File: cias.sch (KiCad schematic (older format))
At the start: 62 parts, among them CN13 KEYBOARD, CN6 SERIAL_DB25M, CN7 PARALLEL_DB25F, Q501 2N3904, Q502 2N3906, Q503 2N3906, Q711 2N3904, U38 MC1488, U39 MC1489, U42 NE555, U7 VIA_8520, U8 VIA_8520

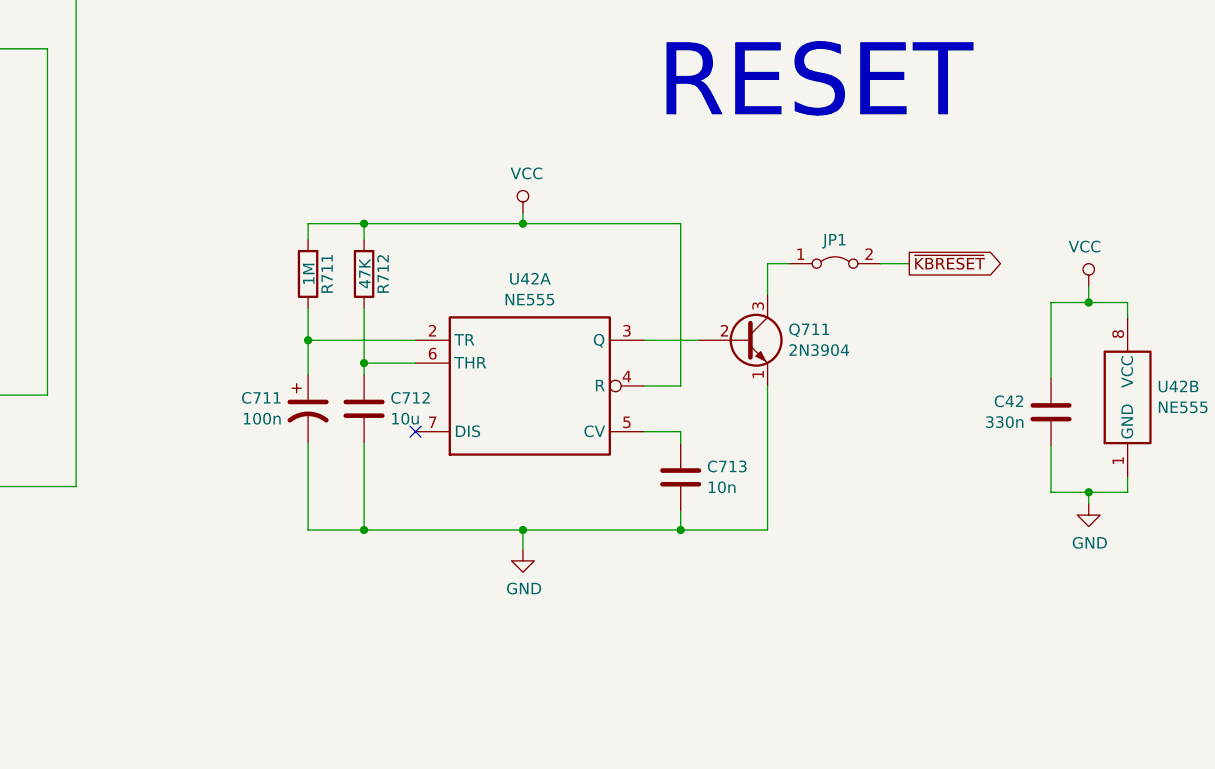
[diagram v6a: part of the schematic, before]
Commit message: Fix power-up reset
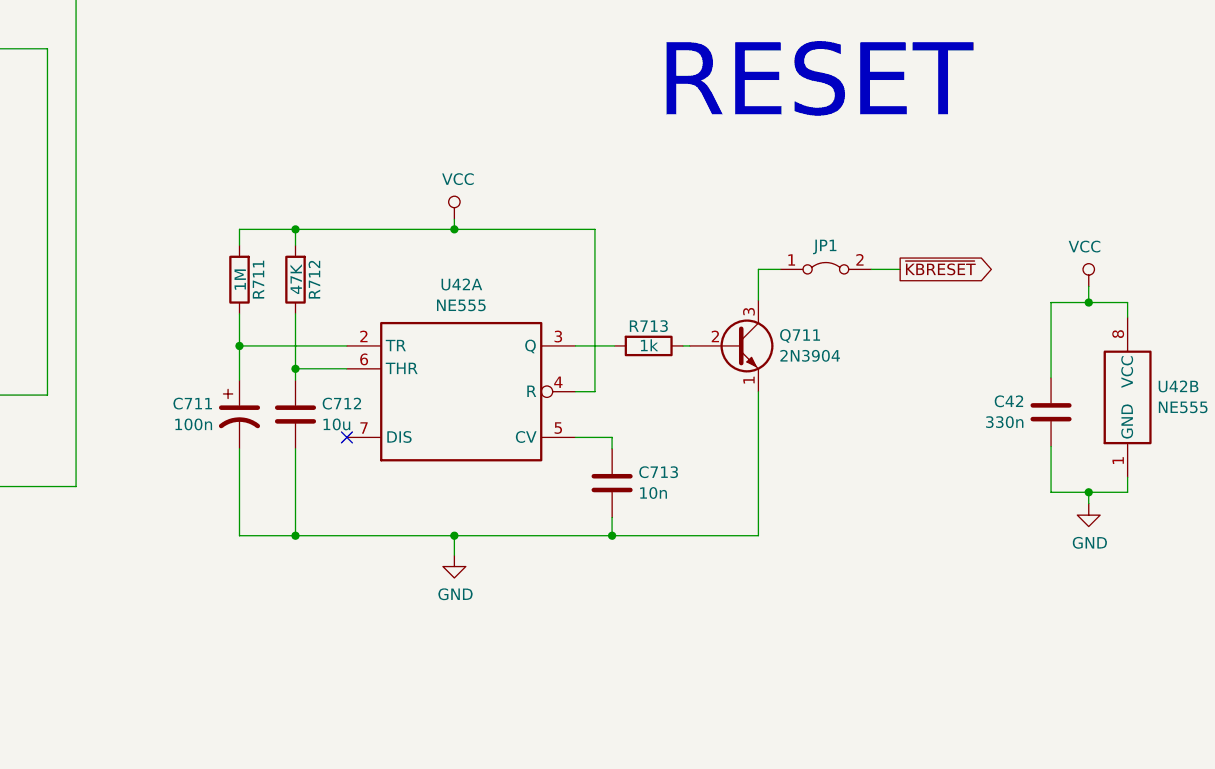
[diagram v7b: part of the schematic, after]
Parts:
- added R713: 1k, Raemixx500:R_Axial_DIN0309_L9.0mm_D3.2mm_P12.70mm_Horizontal, symbol Device:R
- C42, C8: footprint (none) -> Raemixx500:C_Axial_L6.3mm_D2.5mm_P10.16mm
- C711, C713: footprint (none) -> Raemixx500:C_Axial_L9.0mm_D3.2mm_P12.70mm
- Q501, Q502, Q503, Q711: footprint (none) -> Package_TO_SOT_THT:TO-92L_Inline_Wide
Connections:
- net at Q711.2 (B): now also R713.1; no longer U42.3 (Q)
- new net: R713.2, U42.3 (Q)
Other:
- moved on the sheet: C711, C712, C713, JP1, Q711, R711, R712, U42A

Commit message: Work in progress
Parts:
- C39, C501: footprint (none) -> Raemixx500:C_Axial_L9.0mm_D3.2mm_P12.70mm
- C7: footprint (none) -> Raemixx500:C_Axial_L6.3mm_D2.5mm_P10.16mm
- E501, E502, E503: footprint (none) -> Raemixx500:EMI_Filter_Longer
- E511, E512, E513, E514, E515, E516, E517, E518, E519, E520, E521, E522, E523, E524, E531, E538: footprint (none) -> Raemixx500:EMI_Filter_Short
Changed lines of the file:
@@
 F 0 "E501" V 9870 1490 50  0000 C CNN
 F 1 "47" V 9955 1490 50  0000 C CNN
-F 2 "" V 9885 1490 50  0001 C CNN
+F 2 "Raemixx500:EMI_Filter_Longer" V 9885 1490 50  0001 C CNN
 F 3 "~" H 9955 1490 50  0001 C CNN
 	1    9955 1490
@@
 F 0 "E520" H 9950 2195 50  0000 C CNN
 F 1 "470p" H 9825 1935 50  0000 C CNN
-F 2 "" V 9950 1990 50  0001 C CNN
+F 2 "Raemixx500:EMI_Filter_Short" V 9950 1990 50  0001 C CNN
 F 3 "http://www.murata.com/~/media/webrenewal/support/library/catalog/products/emc/emifil/c31e.ashx?la=en-gb" V 9950 1990 50  0001 C CNN
 	1    9950 1990
@@
 F 0 "E511" H 7875 1680 50  0000 C CNN
 F 1 "100p" H 7855 1460 50  0000 C CNN
-F 2 "" V 8045 1490 50  0001 C CNN
+F 2 "Raemixx500:EMI_Filter_Short" V 8045 1490 50  0001 C CNN
 F 3 "http://www.murata.com/~/media/webrenewal/support/library/catalog/products/emc/emifil/c31e.ashx?la=en-gb" V 8045 1490 50  0001 C CNN
 	1    8045 1490
@@
 F 0 "E512" H 8430 1885 50  0000 C CNN
 F 1 "100p" H 8595 1660 50  0000 C CNN
-F 2 "" V 8430 1690 50  0001 C CNN
+F 2 "Raemixx500:EMI_Filter_Short" V 8430 1690 50  0001 C CNN
 F 3 "http://www.murata.com/~/media/webrenewal/support/library/catalog/products/emc/emifil/c31e.ashx?la=en-gb" V 8430 1690 50  0001 C CNN
 	1    8430 1690
@@
 F 0 "E513" H 7875 2080 50  0000 C CNN
 F 1 "100p" H 7855 1865 50  0000 C CNN
-F 2 "" V 8045 1890 50  0001 C CNN
+F 2 "Raemixx500:EMI_Filter_Short" V 8045 1890 50  0001 C CNN
 F 3 "http://www.murata.com/~/media/webrenewal/support/library/catalog/products/emc/emifil/c31e.ashx?la=en-gb" V 8045 1890 50  0001 C CNN
 	1    8045 1890
@@
 F 0 "E514" H 8430 2285 50  0000 C CNN
 F 1 "100p" H 8600 2060 50  0000 C CNN
-F 2 "" V 8430 2090 50  0001 C CNN
+F 2 "Raemixx500:EMI_Filter_Short" V 8430 2090 50  0001 C CNN
 F 3 "http://www.murata.com/~/media/webrenewal/support/library/catalog/products/emc/emifil/c31e.ashx?la=en-gb" V 8430 2090 50  0001 C CNN
 	1    8430 2090
@@
 F 0 "E515" H 8045 2480 50  0000 C CNN
 F 1 "100p" H 7860 2260 50  0000 C CNN
-F 2 "" V 8045 2290 50  0001 C CNN
+F 2 "Raemixx500:EMI_Filter_Short" V 8045 2290 50  0001 C CNN
 F 3 "http://www.murata.com/~/media/webrenewal/support/library/catalog/products/emc/emifil/c31e.ashx?la=en-gb" V 8045 2290 50  0001 C CNN
 	1    8045 2290
@@
 F 0 "E516" H 8430 2690 50  0000 C CNN
 F 1 "100p" H 8595 2465 50  0000 C CNN
-F 2 "" V 8430 2490 50  0001 C CNN
+F 2 "Raemixx500:EMI_Filter_Short" V 8430 2490 50  0001 C CNN
 F 3 "http://www.murata.com/~/media/webrenewal/support/library/catalog/products/emc/emifil/c31e.ashx?la=en-gb" V 8430 2490 50  0001 C CNN
 	1    8430 2490
@@
 F 0 "E517" H 8045 2880 50  0000 C CNN
 F 1 "100p" H 7860 2660 50  0000 C CNN
-F 2 "" V 8045 2690 50  0001 C CNN
+F 2 "Raemixx500:EMI_Filter_Short" V 8045 2690 50  0001 C CNN
 F 3 "http://www.murata.com/~/media/webrenewal/support/library/catalog/products/emc/emifil/c31e.ashx?la=en-gb" V 8045 2690 50  0001 C CNN
 	1    8045 2690
@@
 F 0 "E518" H 8430 3085 50  0000 C CNN
 F 1 "100p" H 8590 2860 50  0000 C CNN
-F 2 "" V 8430 2890 50  0001 C CNN
+F 2 "Raemixx500:EMI_Filter_Short" V 8430 2890 50  0001 C CNN
 F 3 "http://www.murata.com/~/media/webrenewal/support/library/catalog/products/emc/emifil/c31e.ashx?la=en-gb" V 8430 2890 50  0001 C CNN
 	1    8430 2890
@@
 F 0 "E519" H 8045 3280 50  0000 C CNN
 F 1 "100p" H 7850 3060 50  0000 C CNN
-F 2 "" V 8045 3090 50  0001 C CNN
+F 2 "Raemixx500:EMI_Filter_Short" V 8045 3090 50  0001 C CNN
 F 3 "http://www.murata.com/~/media/webrenewal/support/library/catalog/products/emc/emifil/c31e.ashx?la=en-gb" V 8045 3090 50  0001 C CNN
 	1    8045 3090
@@
 F 0 "E521" H 8430 3485 50  0000 C CNN
 F 1 "100p" H 8590 3260 50  0000 C CNN
-F 2 "" V 8430 3290 50  0001 C CNN
+F 2 "Raemixx500:EMI_Filter_Short" V 8430 3290 50  0001 C CNN
 F 3 "http://www.murata.com/~/media/webrenewal/support/library/catalog/products/emc/emifil/c31e.ashx?la=en-gb" V 8430 3290 50  0001 C CNN
 	1    8430 3290
@@
 F 0 "E522" H 8045 3680 50  0000 C CNN
 F 1 "100p" H 7865 3465 50  0000 C CNN
-F 2 "" V 8045 3490 50  0001 C CNN
+F 2 "Raemixx500:EMI_Filter_Short" V 8045 3490 50  0001 C CNN
 F 3 "http://www.murata.com/~/media/webrenewal/support/library/catalog/products/emc/emifil/c31e.ashx?la=en-gb" V 8045 3490 50  0001 C CNN
 	1    8045 3490
@@
 F 0 "E523" H 8430 3885 50  0000 C CNN
 F 1 "100p" H 8595 3665 50  0000 C CNN
-F 2 "" V 8430 3690 50  0001 C CNN
+F 2 "Raemixx500:EMI_Filter_Short" V 8430 3690 50  0001 C CNN
 F 3 "http://www.murata.com/~/media/webrenewal/support/library/catalog/products/emc/emifil/c31e.ashx?la=en-gb" V 8430 3690 50  0001 C CNN
 	1    8430 3690
@@
 F 0 "E524" H 8045 4080 50  0000 C CNN
 F 1 "100p" H 8210 3860 50  0000 C CNN
-F 2 "" V 8045 3890 50  0001 C CNN
+F 2 "Raemixx500:EMI_Filter_Short" V 8045 3890 50  0001 C CNN
 F 3 "http://www.murata.com/~/media/webrenewal/support/library/catalog/products/emc/emifil/c31e.ashx?la=en-gb" V 8045 3890 50  0001 C CNN
 	1    8045 3890
@@
 F 0 "E503" V 8420 8210 50  0000 C CNN
 F 1 "47" V 8505 8210 50  0000 C CNN
-F 2 "" V 8435 8210 50  0001 C CNN
+F 2 "Raemixx500:EMI_Filter_Longer" V 8435 8210 50  0001 C CNN
 F 3 "~" H 8505 8210 50  0001 C CNN
 	1    8505 8210
@@
 F 0 "E502" V 8420 8010 50  0000 C CNN
 F 1 "47" V 8505 8010 50  0000 C CNN
-F 2 "" V 8435 8010 50  0001 C CNN
+F 2 "Raemixx500:EMI_Filter_Longer" V 8435 8010 50  0001 C CNN
 F 3 "~" H 8505 8010 50  0001 C CNN
 	1    8505 8010
@@
 F 0 "C501" V 10165 7310 50  0000 C CNN
 F 1 "330n" V 10005 7180 50  0000 C CNN
-F 2 "" H 10050 7310 50  0001 C CNN
+F 2 "Raemixx500:C_Axial_L9.0mm_D3.2mm_P12.70mm" H 10050 7310 50  0001 C CNN
 F 3 "~" H 10050 7310 50  0001 C CNN
 	1    10050 7310
@@
 F 0 "E531" H 10180 8000 50  0000 C CNN
 F 1 "470p" H 9990 7780 50  0000 C CNN
-F 2 "" V 10180 7810 50  0001 C CNN
+F 2 "Raemixx500:EMI_Filter_Short" V 10180 7810 50  0001 C CNN
 F 3 "http://www.murata.com/~/media/webrenewal/support/library/catalog/products/emc/emifil/c31e.ashx?la=en-gb" V 10180 7810 50  0001 C CNN
 	1    10180 7810
@@
 F 0 "E538" H 10180 8405 50  0000 C CNN
 F 1 "470p" H 9990 8180 50  0000 C CNN
-F 2 "" V 10180 8210 50  0001 C CNN
+F 2 "Raemixx500:EMI_Filter_Short" V 10180 8210 50  0001 C CNN
 F 3 "http://www.murata.com/~/media/webrenewal/support/library/catalog/products/emc/emifil/c31e.ashx?la=en-gb" V 10180 8210 50  0001 C CNN
 	1    10180 8210
@@
 F 0 "C39" H 1305 10406 50  0000 L CNN
 F 1 "10n" H 1305 10315 50  0000 L CNN
-F 2 "" H 1228 10210 50  0001 C CNN
+F 2 "Raemixx500:C_Axial_L9.0mm_D3.2mm_P12.70mm" H 1228 10210 50  0001 C CNN
 F 3 "~" H 1190 10360 50  0001 C CNN
 	1    1190 10360
@@
 F 0 "C7" H 7120 10286 50  0000 L CNN
 F 1 "10n" H 7120 10195 50  0000 L CNN
-F 2 "" H 7043 10090 50  0001 C CNN
+F 2 "Raemixx500:C_Axial_L6.3mm_D2.5mm_P10.16mm" H 7043 10090 50  0001 C CNN
 F 3 "~" H 7005 10240 50  0001 C CNN
 	1    7005 10240
